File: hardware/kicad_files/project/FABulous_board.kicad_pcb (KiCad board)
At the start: 4 copper layers, 101.2 x 63.5 mm, 85 parts, among them J1 Conn_01x03_Pin, J10 Conn_01x07_Pin, J11 Conn_01x03_Pin, J12 Conn_01x03_Pin, J13 Conn_01x03_Pin, J2 Conn_01x03_Pin, J3 Conn_01x03_Pin, J4 Conn_01x03_Pin, J5 Conn_01x02_Pin, J6 Conn_02x04_Odd_Even, J7 Conn_02x12_Odd_Even, J8 Conn_01x03_Pin, J9 Conn_01x05_Pin, SW1 Tactile Switch, T1 LOGO, T2 LOGO, T3 LOGO, T4 LOGO, T5 LOGO, U1 W25Q32JVSSIQ, U10 SN74LVC1G125DCKR, U11 SI5351A-B-GTR, U2 C2977809, U4 GT-USB-7010ASV, U5 FT232H, U6 AMS1117-3_3, U7 SPX1117M3-L_TR, U8 MCP1319MT-29LE-OT, U9 SN74LVC1G125DCKR, X1 TXM12M0004252DBCEO00T, X2 NX3225GA-25_000M-STD-CRG-2

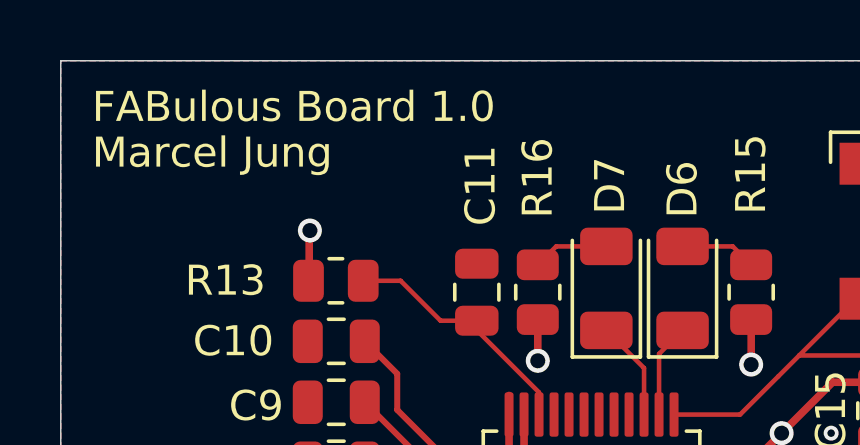
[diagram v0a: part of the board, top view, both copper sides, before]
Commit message: doc: remove creator name and use the page variable for the revision
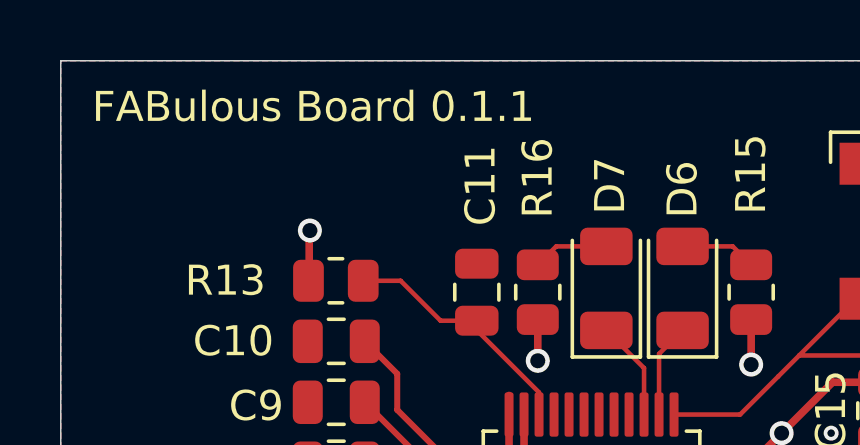
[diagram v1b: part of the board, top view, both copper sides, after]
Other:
- board text added: "FABulous Board ${REVISION}"
- board text removed: "FABulous Board 1.0"
- board text removed: "Marcel Jung"
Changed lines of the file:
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@@
-		)
-	)
-	(gr_text "Marcel Jung"
-		(at 104.648 71.628 0)
-		(layer "F.SilkS")
-		(effects
-			(font
-				(size 1 1)
-				(thickness 0.15)
-			)
-			(justify left bottom)
 		)
 	)
@@
 		)
 	)
-	(gr_text "FABulous Board 1.0"
+	(gr_text "FABulous Board ${REVISION}"
 		(at 104.648 70.104 0)
 		(layer "F.SilkS")
